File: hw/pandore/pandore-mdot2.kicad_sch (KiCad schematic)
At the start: 0 parts

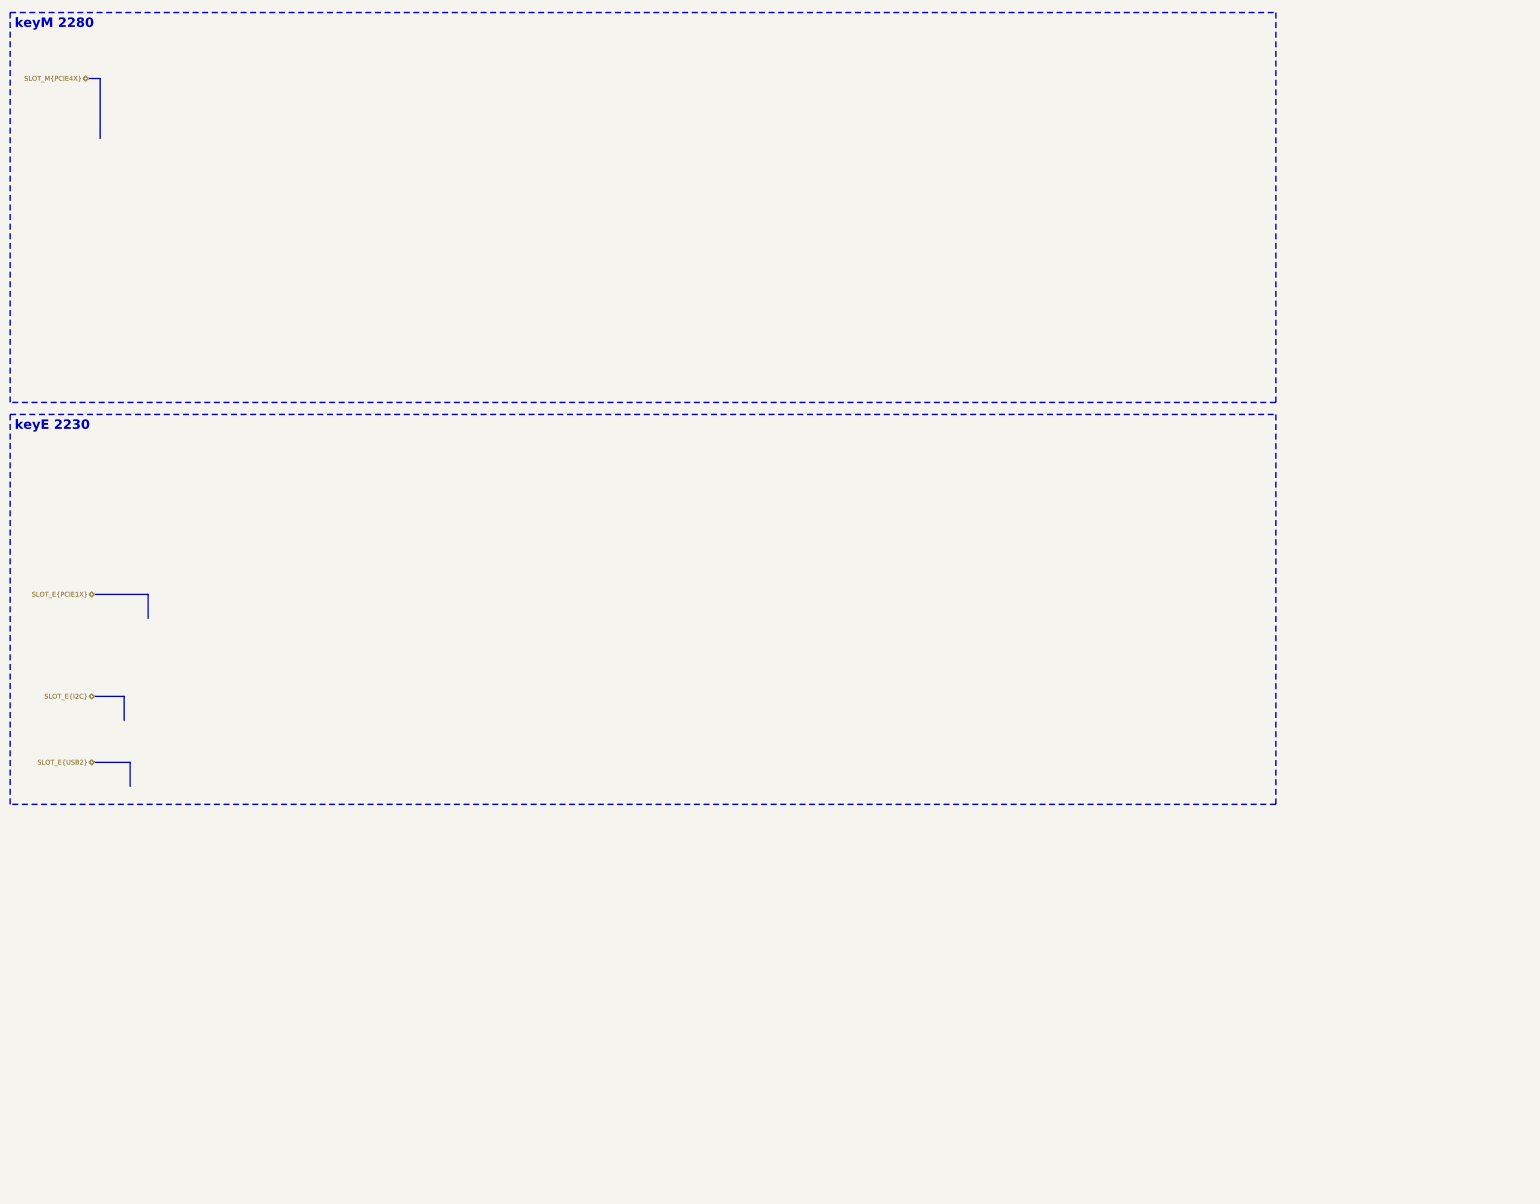
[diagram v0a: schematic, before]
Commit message: Added lots to sch and pcb: eth passive, audio codec, midi, teensy Corrected and added support for M.2
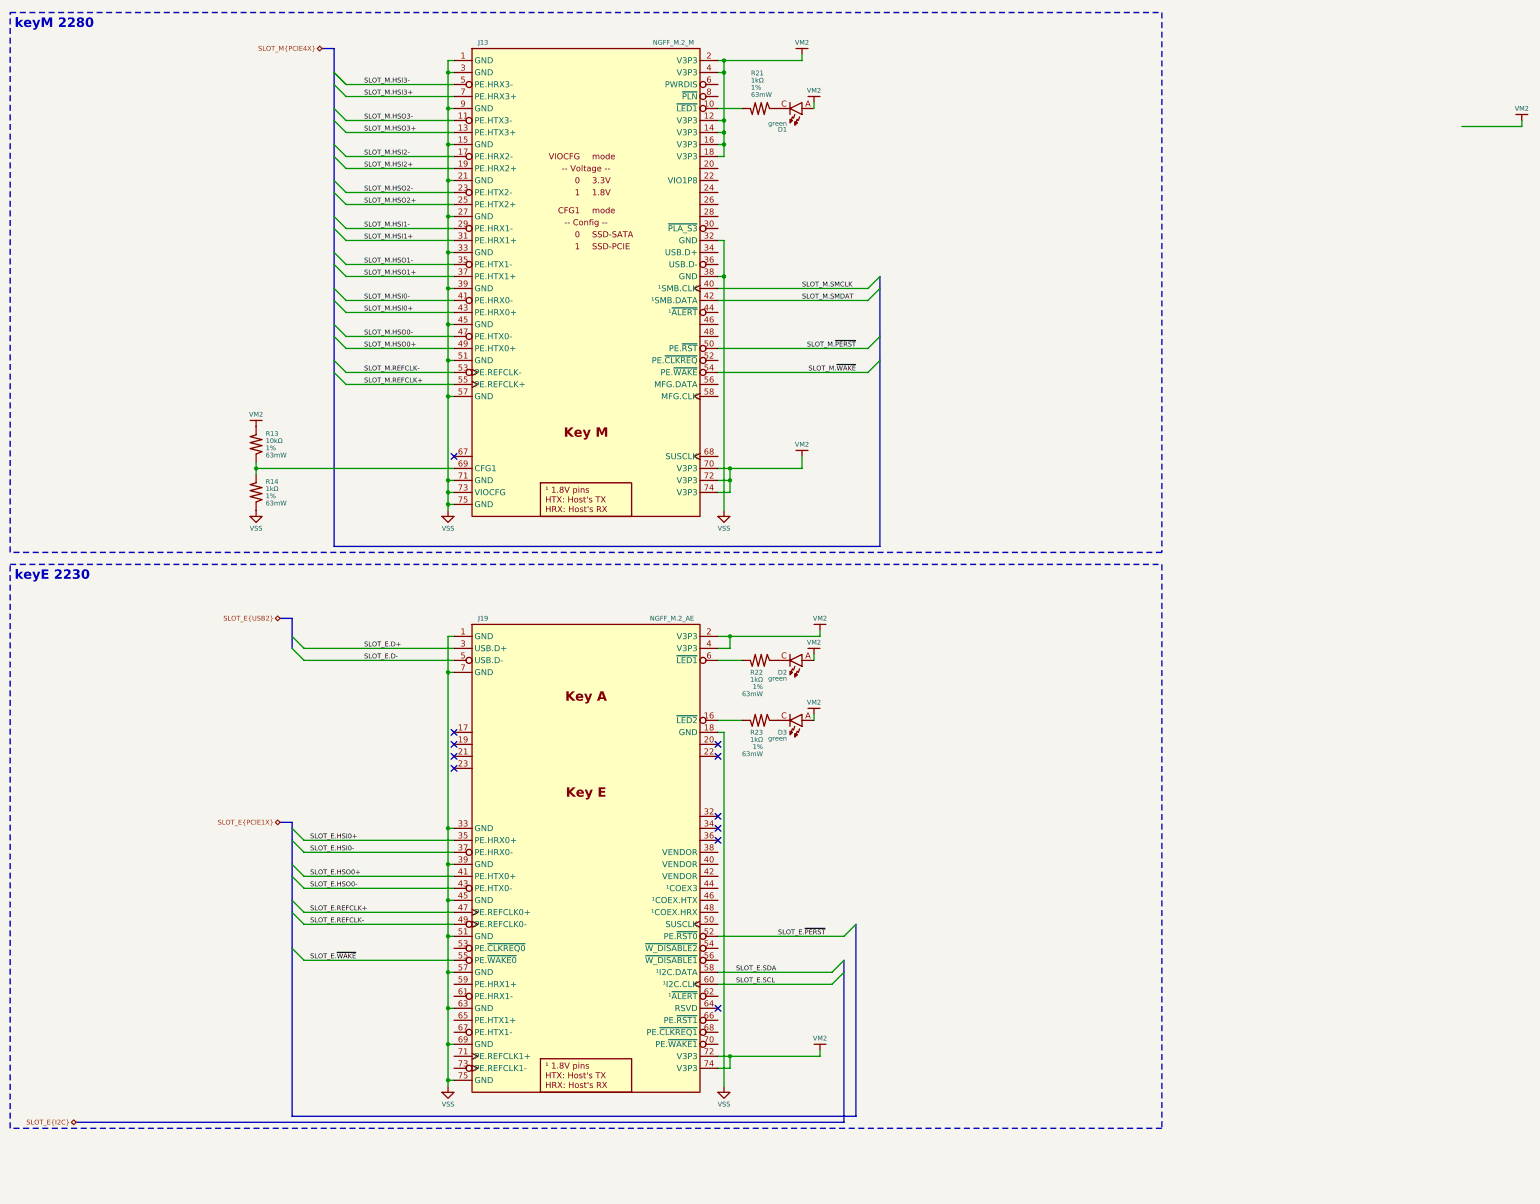
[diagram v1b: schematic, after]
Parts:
- added D1, D2, D3: ${color}, reekilib_led:LEDM1608X80, symbol reekilib_led:led
- added J13: NGFF_M.2_M, reekilib_con:NGFF_M.2_CONN, symbol reekilib_con:NGFF_M.2_M
- added J19: NGFF_M.2_AE, reekilib_con:NGFF_M.2_CONN, symbol reekilib_con:NGFF_M.2_AE
- added R13, R14, R21, R22, R23: ${Resistance}, ${Tolerance}, ${Power}, reekilib_res:RESC1005, symbol reekilib_res:res
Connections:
- new net: J19.16 (~{LED2}), R23.1
- new net: D3.C, R23.2
- new net: J13.10 (~{LED1}), R21.1
- new net: D1.C, R21.2
- new net: J19.6 (~{LED1}), R22.1
- new net: D2.C, R22.2
- new net: J13.69 (CFG1), R13.2, R14.1
- new net SLOT_E.D+: J19.3 (USB.D+)
- new net SLOT_E.D-: J19.5 (USB.D-)
- new net SLOT_E.HSI0+: J19.35 (PE.HRX0+)
- new net SLOT_E.HSI0-: J19.37 (PE.HRX0-)
- new net SLOT_E.HSO0+: J19.41 (PE.HTX0+)
- new net SLOT_E.HSO0-: J19.43 (PE.HTX0-)
- new net SLOT_E.REFCLK+: J19.47 (PE.REFCLK0+)
- new net SLOT_E.REFCLK-: J19.49 (PE.REFCLK0-)
- new net SLOT_E.SCL: J19.60 (¹I2C.CLK)
- new net SLOT_E.SDA: J19.58 (¹I2C.DATA)
- new net SLOT_E.~{PERST}: J19.52 (PE.~{RST0})
- new net SLOT_E.~{WAKE}: J19.55 (PE.~{WAKE0})
- new net SLOT_M.HSI0+: J13.43 (PE.HRX0+)
- new net SLOT_M.HSI0-: J13.41 (PE.HRX0-)
- new net SLOT_M.HSI1+: J13.31 (PE.HRX1+)
- new net SLOT_M.HSI1-: J13.29 (PE.HRX1-)
- new net SLOT_M.HSI2+: J13.19 (PE.HRX2+)
- new net SLOT_M.HSI2-: J13.17 (PE.HRX2-)
- new net SLOT_M.HSI3+: J13.7 (PE.HRX3+)
- new net SLOT_M.HSI3-: J13.5 (PE.HRX3-)
- new net SLOT_M.HSO0+: J13.49 (PE.HTX0+)
- new net SLOT_M.HSO0-: J13.47 (PE.HTX0-)
- new net SLOT_M.HSO1+: J13.37 (PE.HTX1+)
- new net SLOT_M.HSO1-: J13.35 (PE.HTX1-)
- new net SLOT_M.HSO2+: J13.25 (PE.HTX2+)
- new net SLOT_M.HSO2-: J13.23 (PE.HTX2-)
- new net SLOT_M.HSO3+: J13.13 (PE.HTX3+)
- new net SLOT_M.HSO3-: J13.11 (PE.HTX3-)
- new net SLOT_M.REFCLK+: J13.55 (PE.REFCLK+)
- new net SLOT_M.REFCLK-: J13.53 (PE.REFCLK-)
- new net SLOT_M.SMCLK: J13.40 (¹SMB.CLK)
- new net SLOT_M.SMDAT: J13.42 (¹SMB.DATA)
- new net SLOT_M.~{PERST}: J13.50 (PE.~{RST})
- new net SLOT_M.~{WAKE}: J13.54 (PE.~{WAKE})
- new net VM2: D1.A, D2.A, D3.A, J13.12 (V3P3), J13.14 (V3P3), J13.16 (V3P3), J13.18 (V3P3), J13.2 (V3P3), J13.4 (V3P3), J13.70 (V3P3), J13.72 (V3P3), J13.74 (V3P3), J19.2 (V3P3), J19.4 (V3P3), J19.72 (V3P3), J19.74 (V3P3), R13.1
- new net VSS: J13.1 (GND), J13.15 (GND), J13.21 (GND), J13.27 (GND), J13.3 (GND), J13.32 (GND), J13.33 (GND), J13.38 (GND), J13.39 (GND), J13.45 (GND), J13.51 (GND), J13.57 (GND), J13.71 (GND), J13.73 (VIOCFG), J13.75 (GND), J13.9 (GND), J19.1 (GND), J19.18 (GND), J19.33 (GND), J19.39 (GND), J19.45 (GND), J19.51 (GND), J19.57 (GND), J19.63 (GND), J19.69 (GND), J19.7 (GND), J19.75 (GND), R14.2
- no-connect marks 0 -> 11

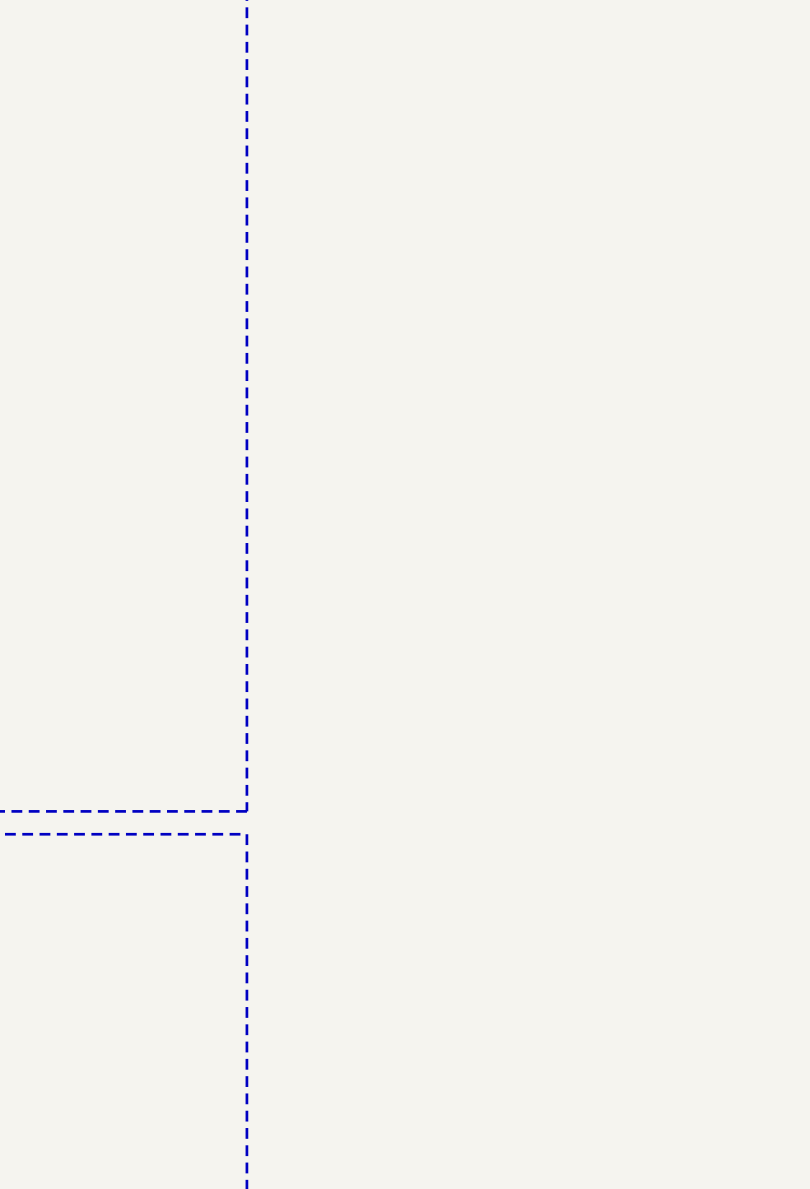
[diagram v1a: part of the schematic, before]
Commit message: added power stuff revised M.2 for higher model and added m.2 mounts added power tap terminals
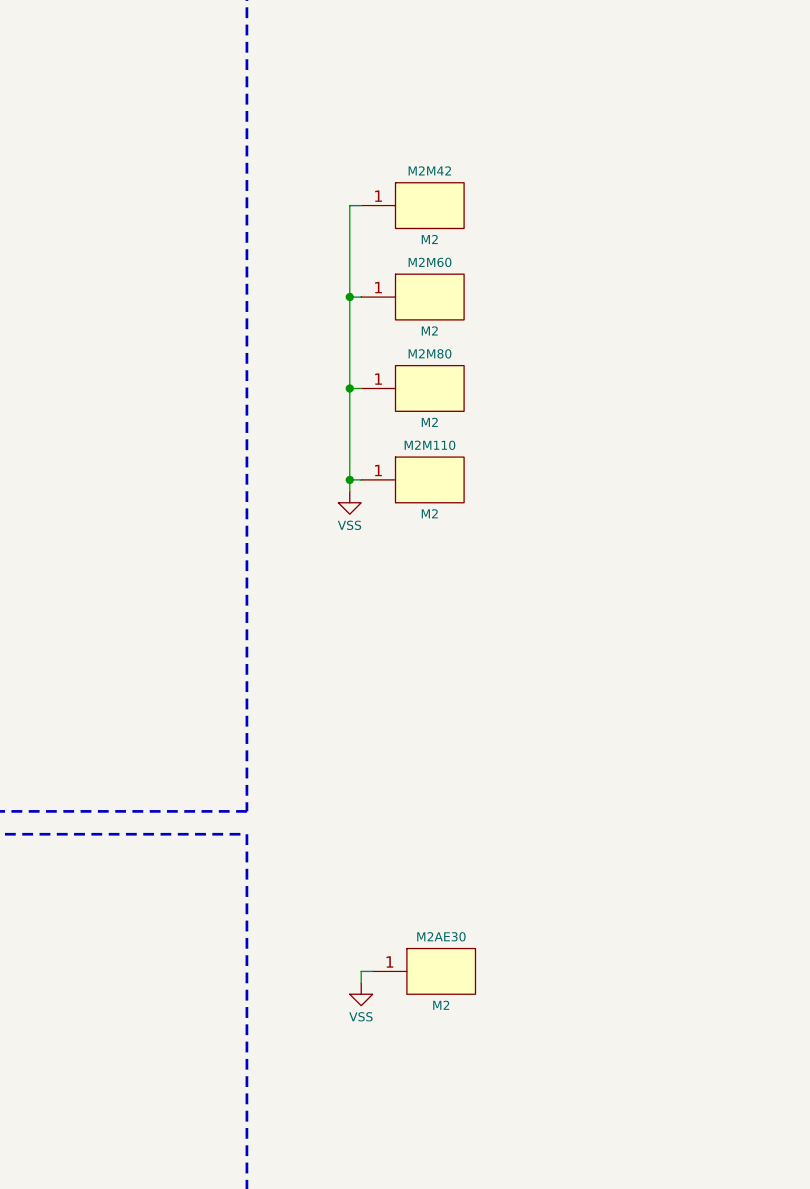
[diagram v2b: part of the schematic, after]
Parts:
- added M2AE30, M2M110, M2M42, M2M60, M2M80: M2, reekilib_mnt:mnt_M2_ele, symbol reekilib_con:hdr-1x1
- J13: Link https://www.te.com/en/product-1-2199230-5.html -> https://www.amphenol-cs.com/product/10131758005rlf.html; Link2 https://www.te.com/en/product-1-2199230-6.html -> (none); Link3 https://www.jae.com/en/connectors/series/detail/product/id=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 -> (none); Link4 https://www.amphenol-cs.com/product/mdt420m01001.html -> (none); Link5 https://www.jae.com/en/connectors/series/detail/product/id=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 -> (none); Link6 https://www.te.com/en/product-1-2199119-5.html -> (none); Link7 https://app.adam-tech.com/products/download/data_sheet/2396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 -> (none); MFG TE -> Amphenol; MFG2 TE -> (none); MFG3 JAE -> (none); MFG4 Amphenol -> (none); MFG5 JAE -> (none); MFG6 TE -> (none); MFG7 Adam Tech -> (none); MPN 1-2199230-5 -> 10131758-005RLF; MPN2 1-2199230-6 -> (none); MPN3 SM3ZS067U410AMR1000 -> (none); MPN4 MDT420M01001 -> (none); MPN5 SM3ZS067U310AMR1200 -> (none); MPN6 1-2199119-5 -> (none); MPN7 M2-A1-67-R-SMT-8.5-KM-T/R -> (none)
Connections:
- net VSS: now also M2AE30.1, M2M110.1, M2M42.1, M2M60.1, M2M80.1
